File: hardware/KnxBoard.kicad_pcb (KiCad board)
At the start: 4 copper layers, 40 parts, among them J1 Conn_01x10, J2 Conn_01x12, J3 Conn_01x12, J4 Conn_01x02_Male, SW1 SW_Push, SW2 SW_Push, U1 NCN5130, U2 STM32L432KCUx, X1 FA-238

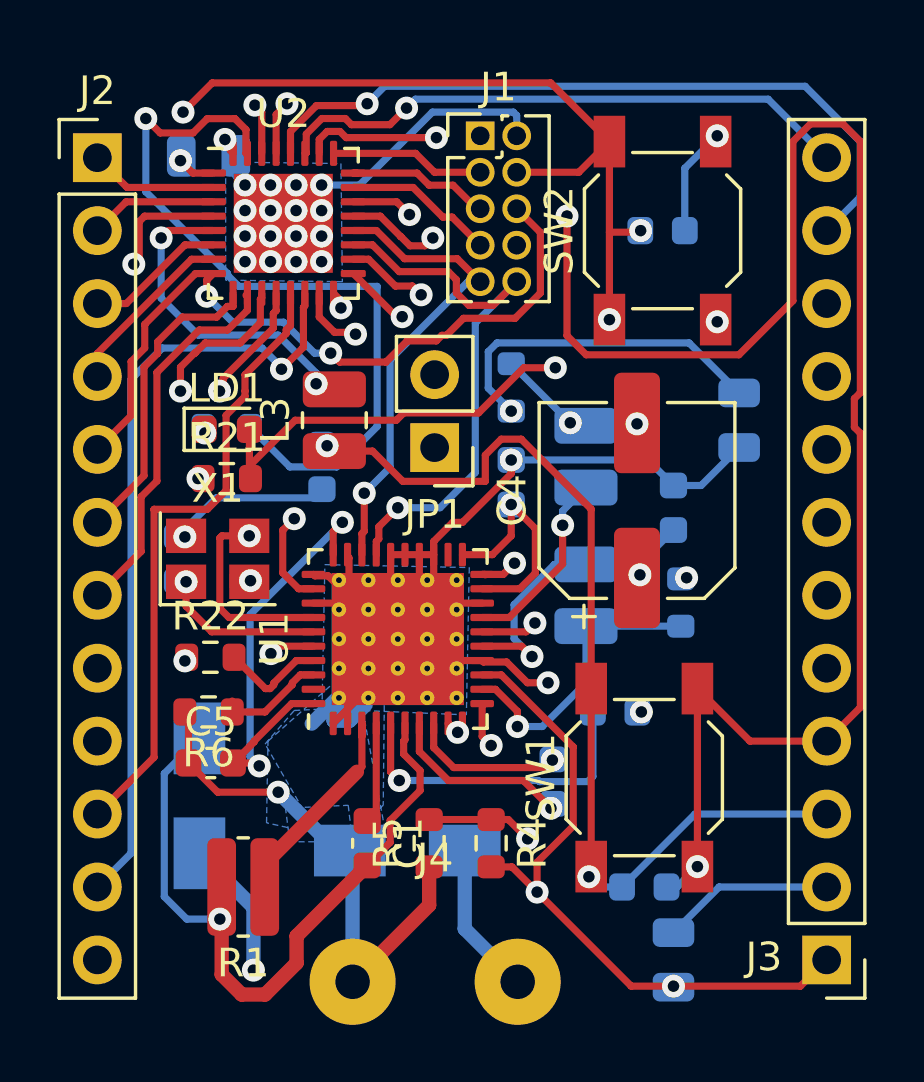
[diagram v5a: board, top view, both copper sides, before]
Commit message: Update serigraphie
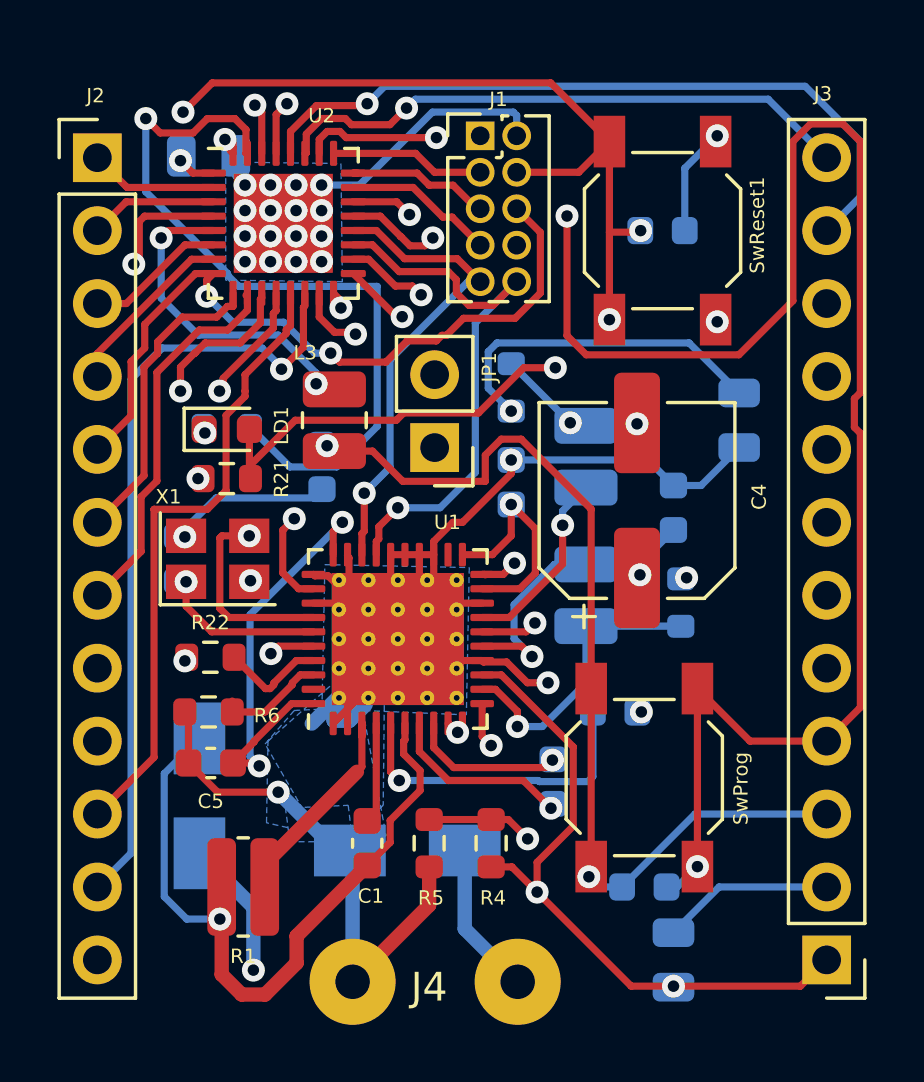
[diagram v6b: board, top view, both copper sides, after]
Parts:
- renumbered SW1 to SwProg, SW2 to SwReset1

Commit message: Add text
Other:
- board text added: "CLK16"
- board text added: "PA1"
- board text added: "PC14"
- board text added: "PC15"
- board text added: "UART_TX"

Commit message: Add text for pin background
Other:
- board text added: "12V"
- board text added: "GND"
- board text added: "LED"
- board text added: "NRST"
- board text added: "PA11"
- board text added: "PA3"
- board text added: "PA4"
- board text added: "PA5"
- board text added: "PA6"
- board text added: "PA7"
- board text added: "PA8"
- board text added: "PB0"
- board text added: "PB1"
- board text added: "PB4"
- board text added: "PB5"
- board text added: "PB6"
- board text added: "PB7"
- board text added: "Prog"
- board text added: "VDD"
